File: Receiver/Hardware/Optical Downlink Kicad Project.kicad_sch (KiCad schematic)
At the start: 16 parts, among them J1 Conn_01x20_Socket, J2 Conn_01x20_Socket, U1 OPA657U, U2 TLE2426-EP_D_8, U3 OPA657U, U4 ADS8691IPWR, U5 MEV3S0515SC

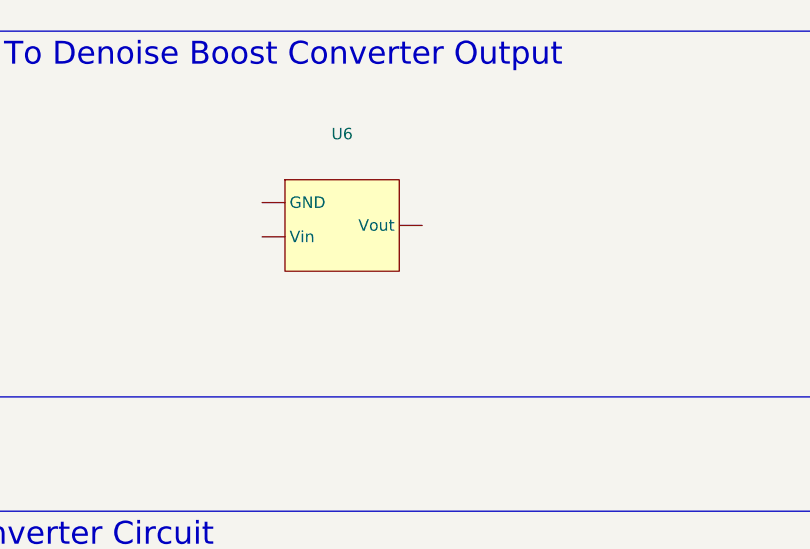
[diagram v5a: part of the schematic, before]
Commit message: Worked on the layout of Optical Downlink
Fixed the layout also added in packages for LDO and boost converter. Need to fix net problems in kicad.
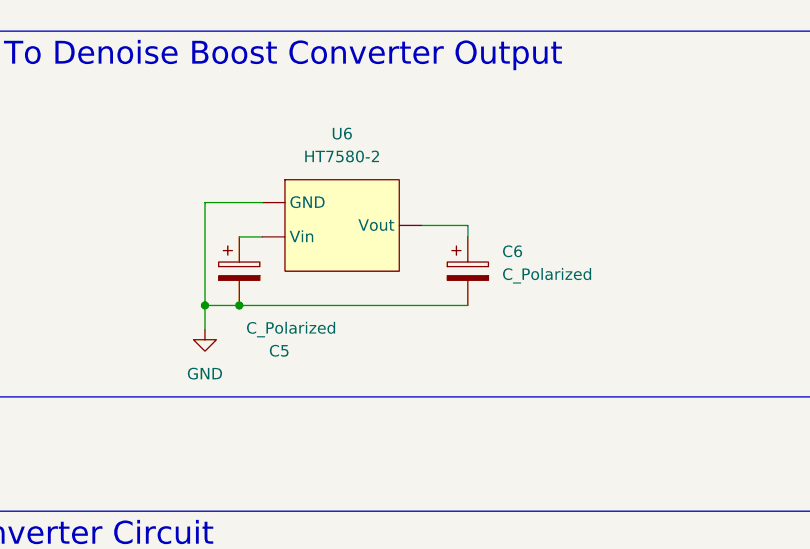
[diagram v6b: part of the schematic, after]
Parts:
- added C5, C6: C_Polarized, Capacitor_Tantalum_SMD:CP_EIA-1608-08_AVX-J, symbol Device:C_Polarized
- U6: value ~ -> HT7580-2; footprint (none) -> Package_TO_SOT_SMD:SOT-23-5
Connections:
- net GND: now also U6. (NC), C5.2, C6.2
- new net: C6.1, U6. (NC)
- new net: C5.1, U6. (NC)

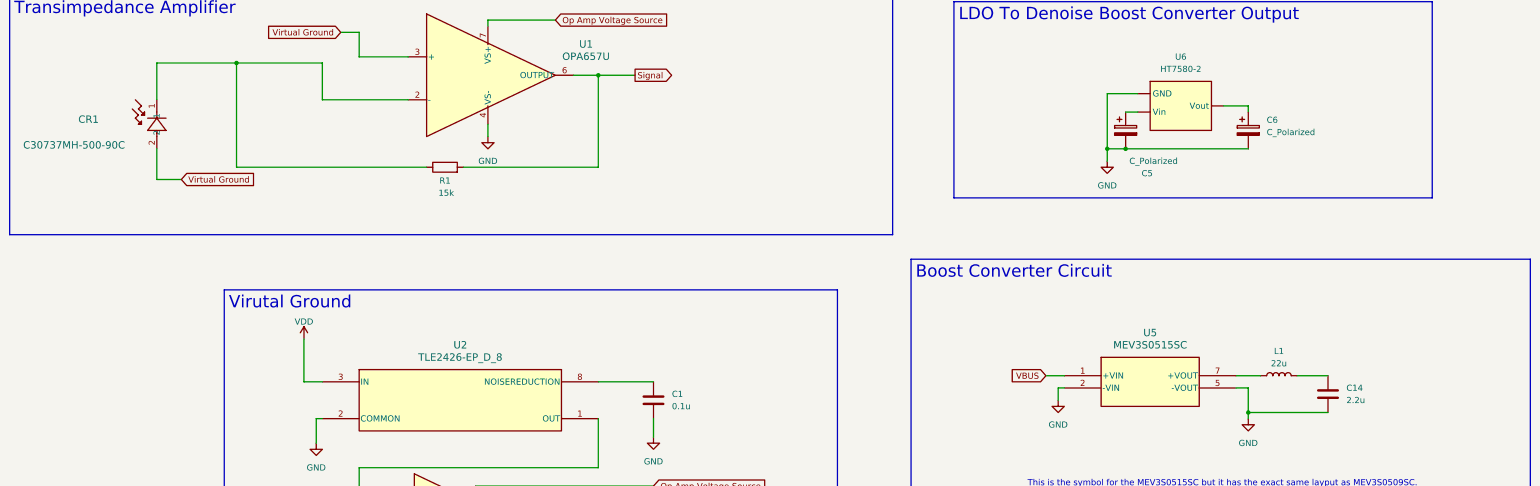
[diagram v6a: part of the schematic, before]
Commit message: Began PCB layout
Also fixed some schematic issues.
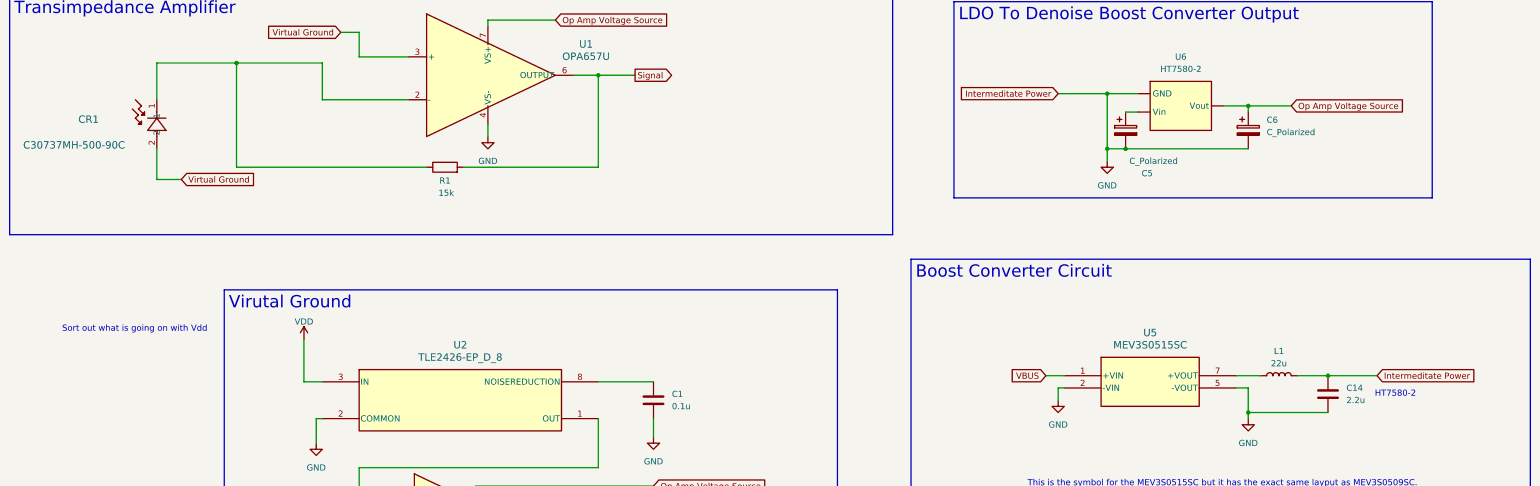
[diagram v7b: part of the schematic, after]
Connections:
- net GND: now also C14.1, L1.2
- net Op Amp Voltage Source: now also C6.1, U6. (NC)
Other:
- note added: "HT7580-2"
- note added: "Sort out what is going on with Vdd"
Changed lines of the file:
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@@
+		)
+	)
+	(text "Sort out what is going on with Vdd"
+		(exclude_from_sim no)
+		(at 43.688 86.868 0)
+		(effects
+			(font
+				(size 1.27 1.27)
+			)
 		)
 	)
@@
 		(exclude_from_sim no)
 		(at 306.324 155.702 0)
+		(effects
+			(font
+				(size 1.27 1.27)
+			)
+		)
+	)
+	(text "HT7580-2"
+		(exclude_from_sim no)
+		(at 304.8 100.33 0)
 		(effects
 			(font
@@
 	)
 	(junction
+		(at 290.83 96.52)
+		(diameter 0)
+		(color 0 0 0 0)
+	)
+	(junction
 		(at 248.92 49.53)
 		(diameter 0)
@@
 	(junction
 		(at 245.11 49.53)
+		(diameter 0)
+		(color 0 0 0 0)
+	)
+	(junction
+		(at 274.32 40.64)
+		(diameter 0)
+		(color 0 0 0 0)
+	)
+	(junction
+		(at 245.11 38.1)
 		(diameter 0)
 		(color 0 0 0 0)
@@
 	(wire
 		(pts
+			(xy 274.32 40.64) (xy 283.21 40.64)
+		)
+		(stroke
+			(width 0)
+			(type default)
+		)
+	)
+	(wire
+		(pts
 			(xy 274.32 104.14) (xy 274.32 105.41)
 		)
@@
 	(wire
 		(pts
+			(xy 234.95 38.1) (xy 245.11 38.1)
+		)
+		(stroke
+			(width 0)
+			(type default)
+		)
+	)
+	(wire
+		(pts
 			(xy 116.84 22.86) (xy 116.84 24.13)
 		)
@@
 		(pts
 			(xy 104.14 180.34) (xy 99.06 180.34)
+		)
+		(stroke
+			(width 0)
+			(type default)
+		)
+	)
+	(wire
+		(pts
+			(xy 290.83 96.52) (xy 300.99 96.52)
 		)
 		(stroke
@@
 		)
 	)
+	(global_label "Intermeditate Power"
+		(shape input)
+		(at 300.99 96.52 0)
+		(fields_autoplaced yes)
+		(effects
+			(font
+				(size 1.27 1.27)
+			)
+			(justify left)
+		)
+		(property "Intersheetrefs" "${INTERSHEET_REFS}"
+			(at 323.1461 96.52 0)
+			(effects
+				(font
+					(size 1.27 1.27)
+				)
+				(justify left)
+				(hide yes)
+			)
+		)
+	)
+	(global_label "Op Amp Voltage Source"
+		(shape input)
+		(at 283.21 40.64 0)
+		(fields_autoplaced yes)
+		(effects
+			(font
+				(size 1.27 1.27)
+			)
+			(justify left)
+		)
+		(property "Intersheetrefs" "${INTERSHEET_REFS}"
+			(at 308.9944 40.64 0)
+			(effects
+				(font
+					(size 1.27 1.27)
+				)
+				(justify left)
+				(hide yes)
+			)
+		)
+	)
 	(global_label "Signal"
 		(shape output)
@@
 				(hide yes)
 			)
+		)
+	)
+	(global_label "Intermeditate Power"
+		(shape input)
+		(at 234.95 38.1 180)
+		(fields_autoplaced yes)
+		(effects
+			(font
+				(size 1.27 1.27)
+			)
+			(justify right)
+		)
+		(property "Intersheetrefs" "${INTERSHEET_REFS}"
+			(at 212.7939 38.1 0)
+			(effects
+				(font
+					(size 1.27 1.27)
+				)
+				(justify right)
+				(hide yes)
+			)

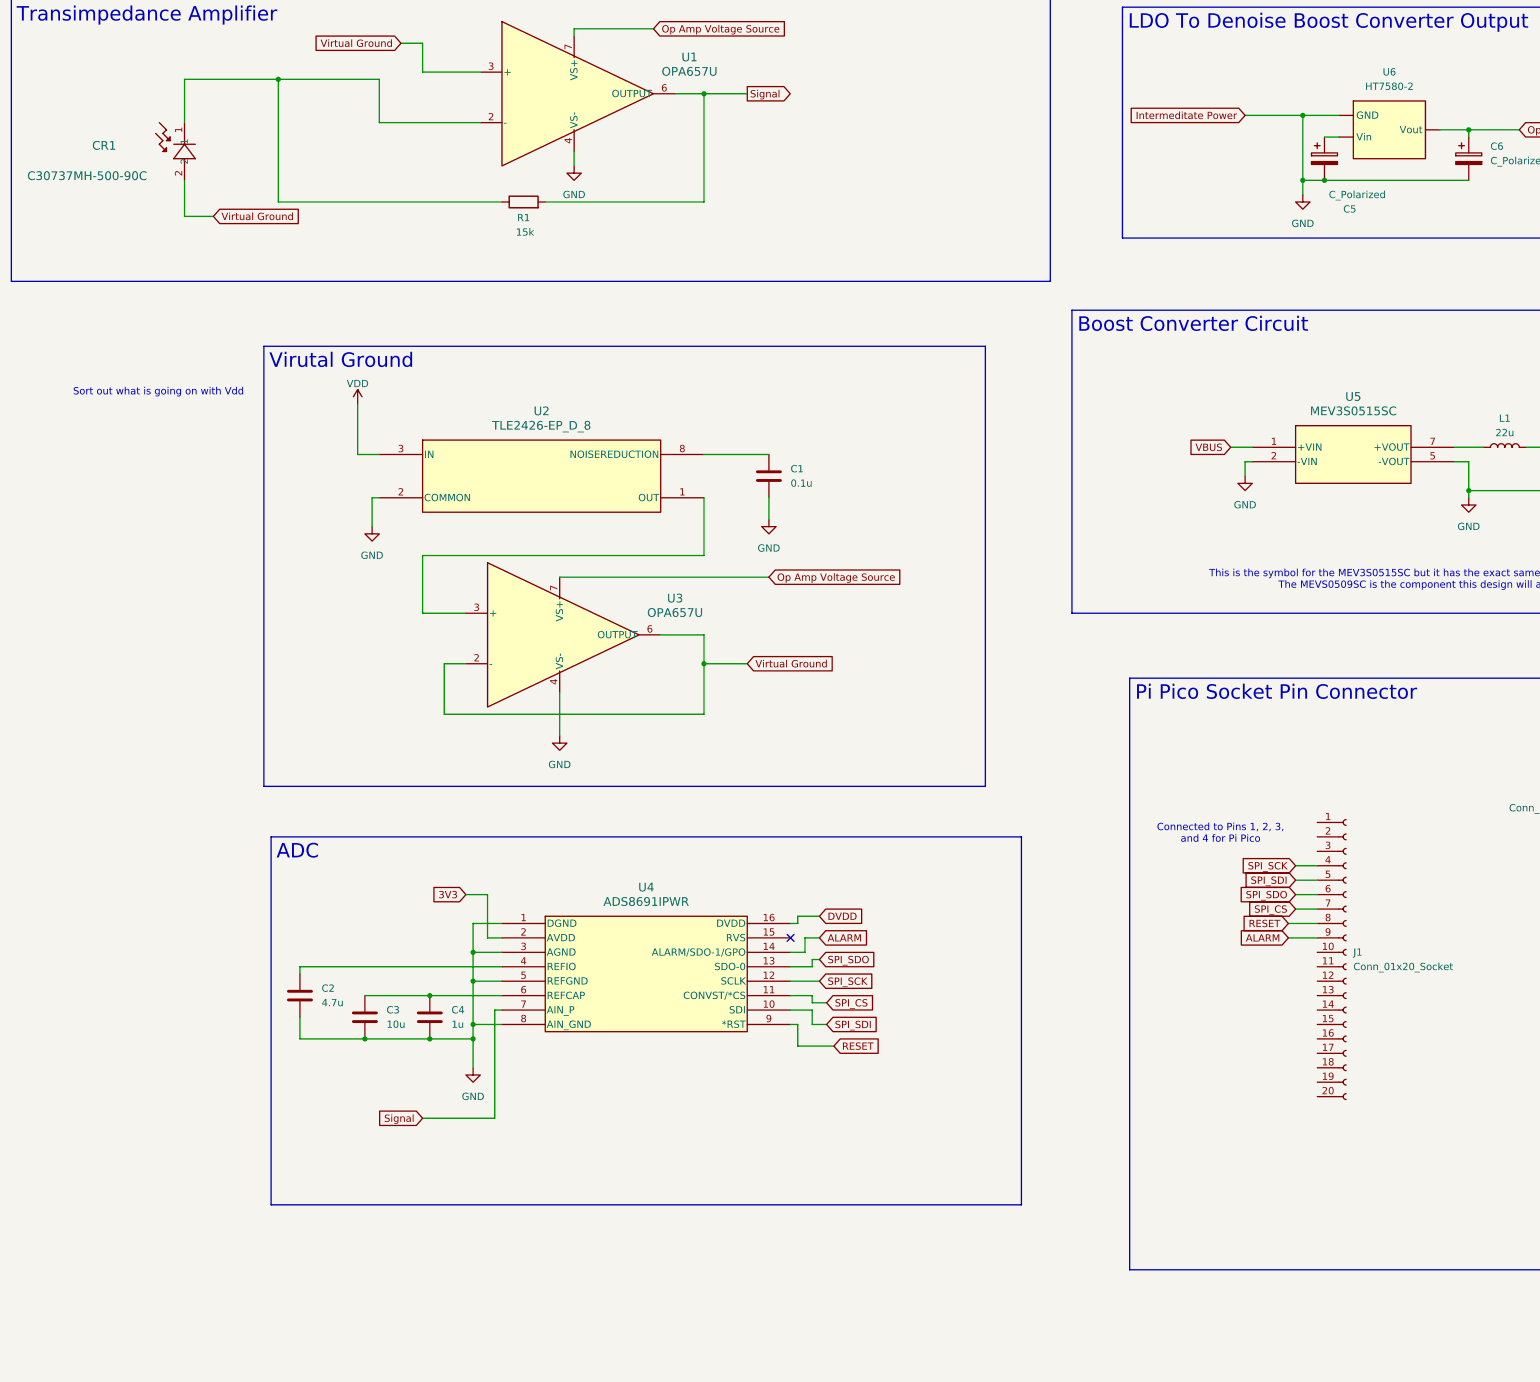
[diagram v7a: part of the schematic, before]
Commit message: Worked on Assigning capacitor and resistors components
Specifically feedback resistor and worked on capacitor in virtual ground circuit.
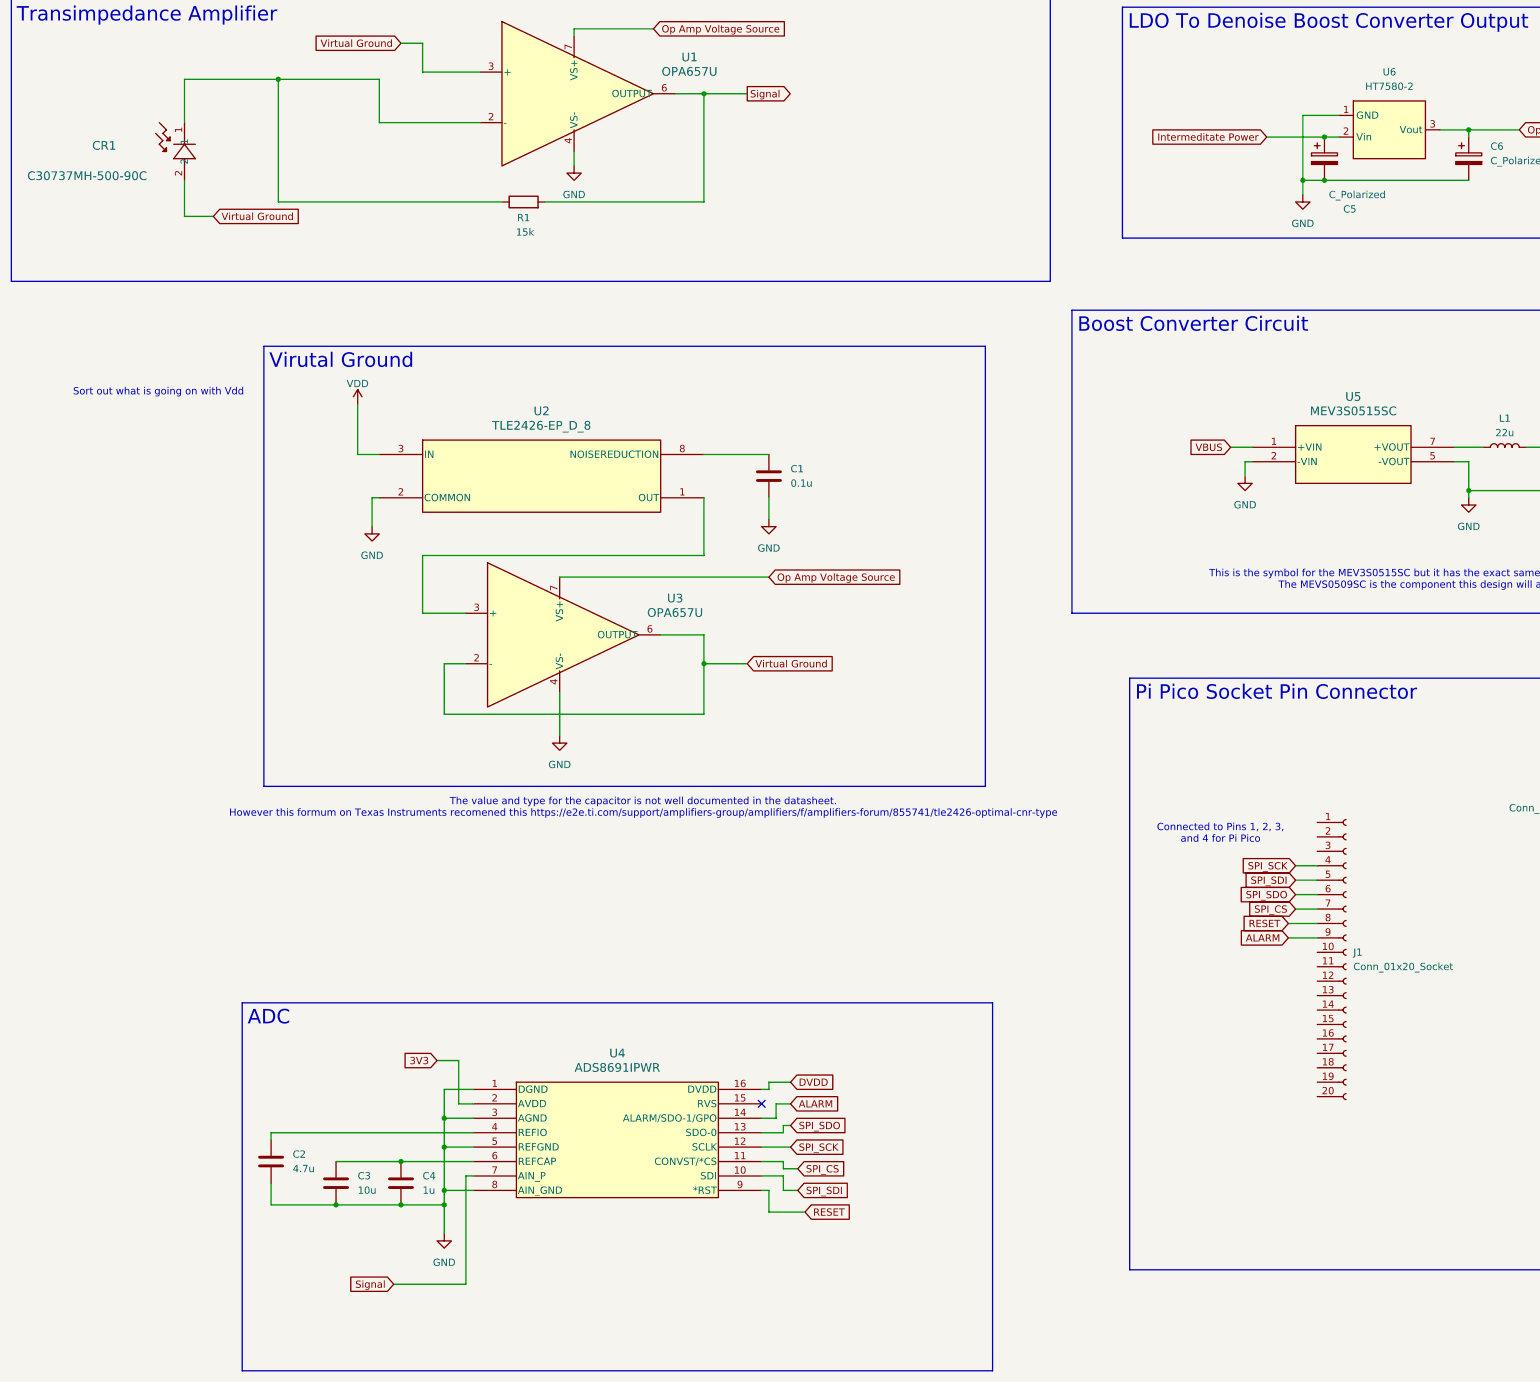
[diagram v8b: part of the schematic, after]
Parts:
- L1: footprint Inductor_SMD:L_6.3x6.3_H3 -> 00-footprint-library:IND_8400_84XXXC_MUR
- R1: footprint Resistor_SMD:R_0201_0603Metric -> 00-footprint-library:RC0402N_YAG
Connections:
- net GND: now also U6.1 (GND); no longer C14.1, L1.2, U6. (NC)
- net Op Amp Voltage Source: now also U6.3 (Vout); no longer U6. (NC)
- net Intermeditate Power: now reaches C5.1
- net Intermeditate Power: now also C14.1, L1.2, U6.2 (Vin); no longer U6. (NC)
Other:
- note added: "The value and type for the capacitor is not well documented in the datasheet. However this formum on Texas Instruments recomened this https://e2e.ti.com/support/amplifiers-group/amplifiers/f/amplifiers-forum/855741/tle2426-optimal-cnr-type"
- moved on the sheet: C2, C3, C4, U4
